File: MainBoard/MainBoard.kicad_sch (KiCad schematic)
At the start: 30 parts, among them U1 V3S, U5 10104110-0001LF, X1 FC-12M32.768KHZ7PF20PPM, X2 X322524MOB4SI

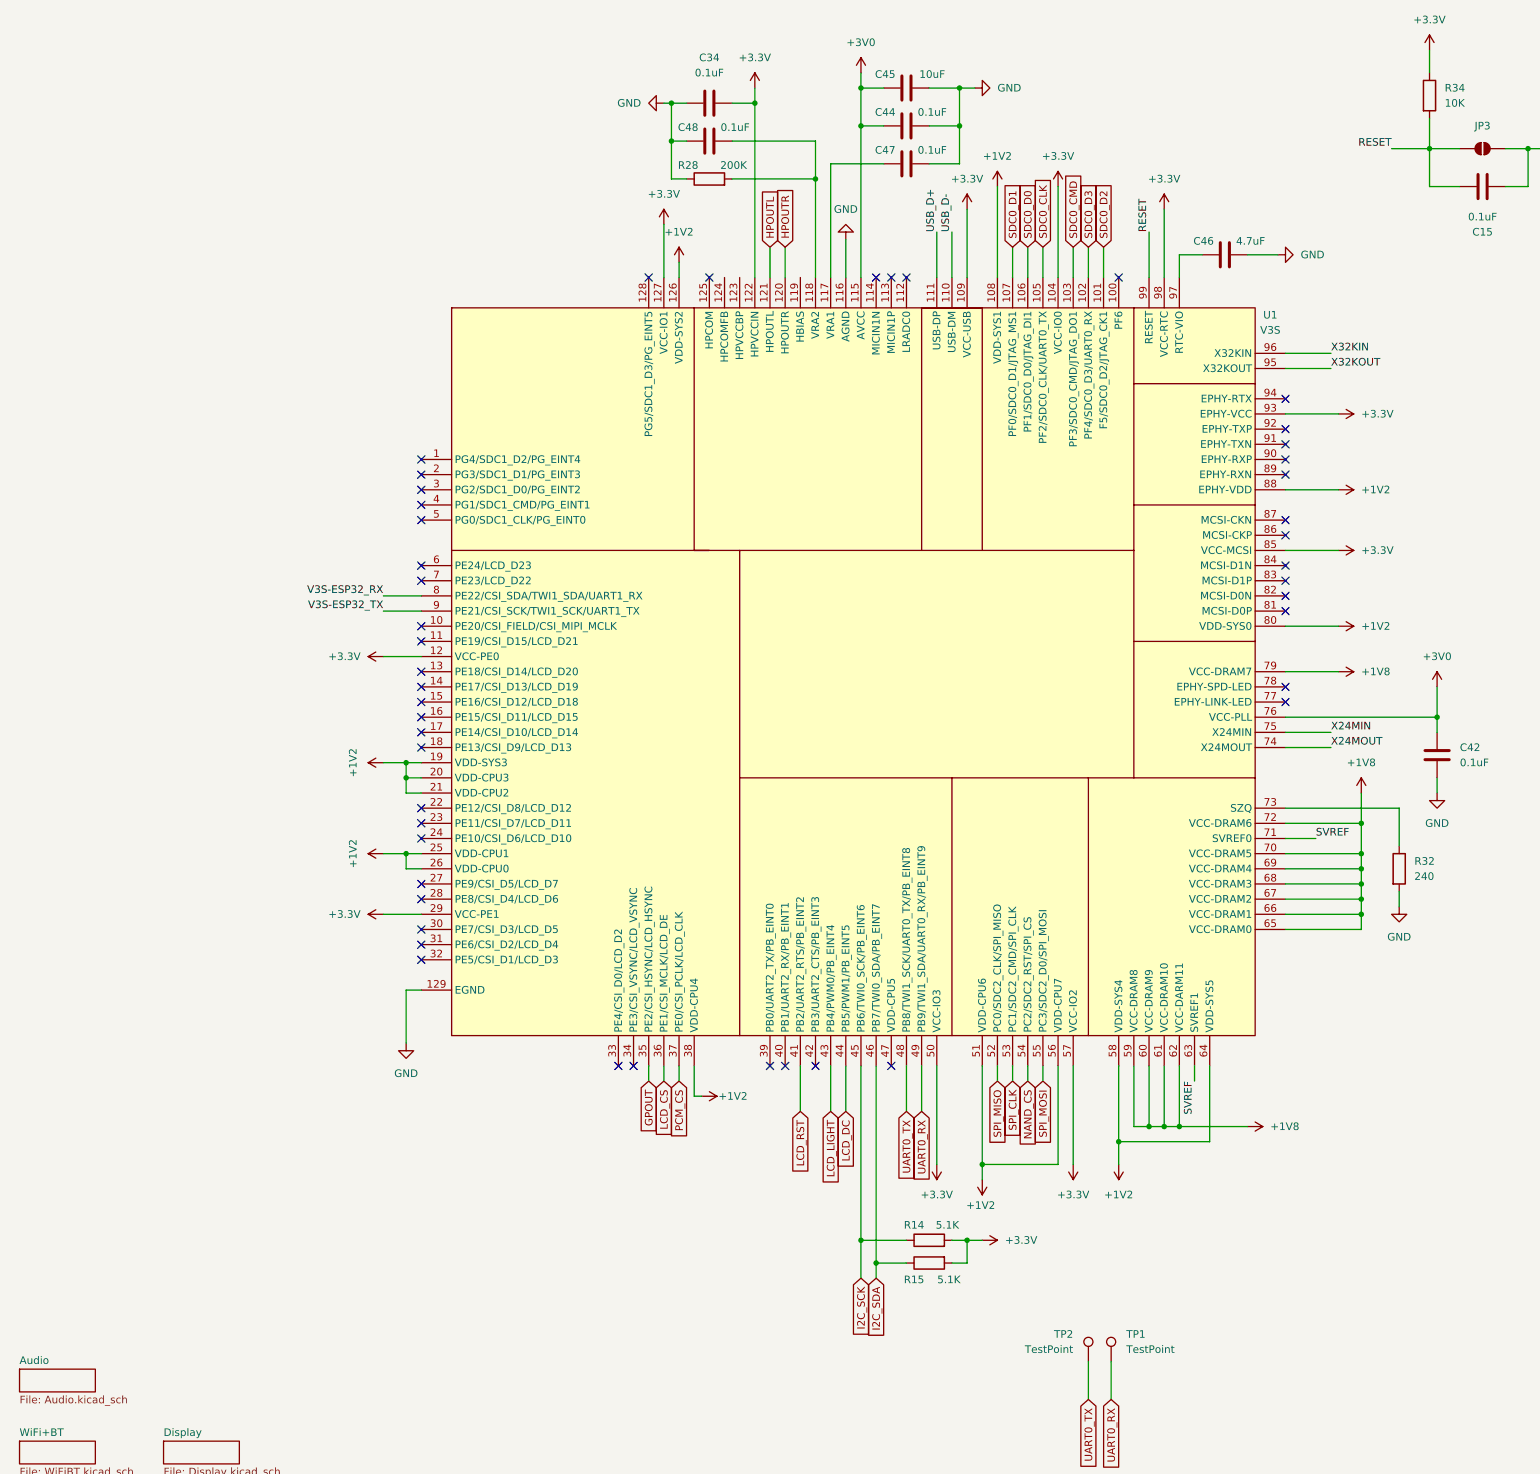
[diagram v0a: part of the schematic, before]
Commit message: footprints for wheel + power changes for v3s
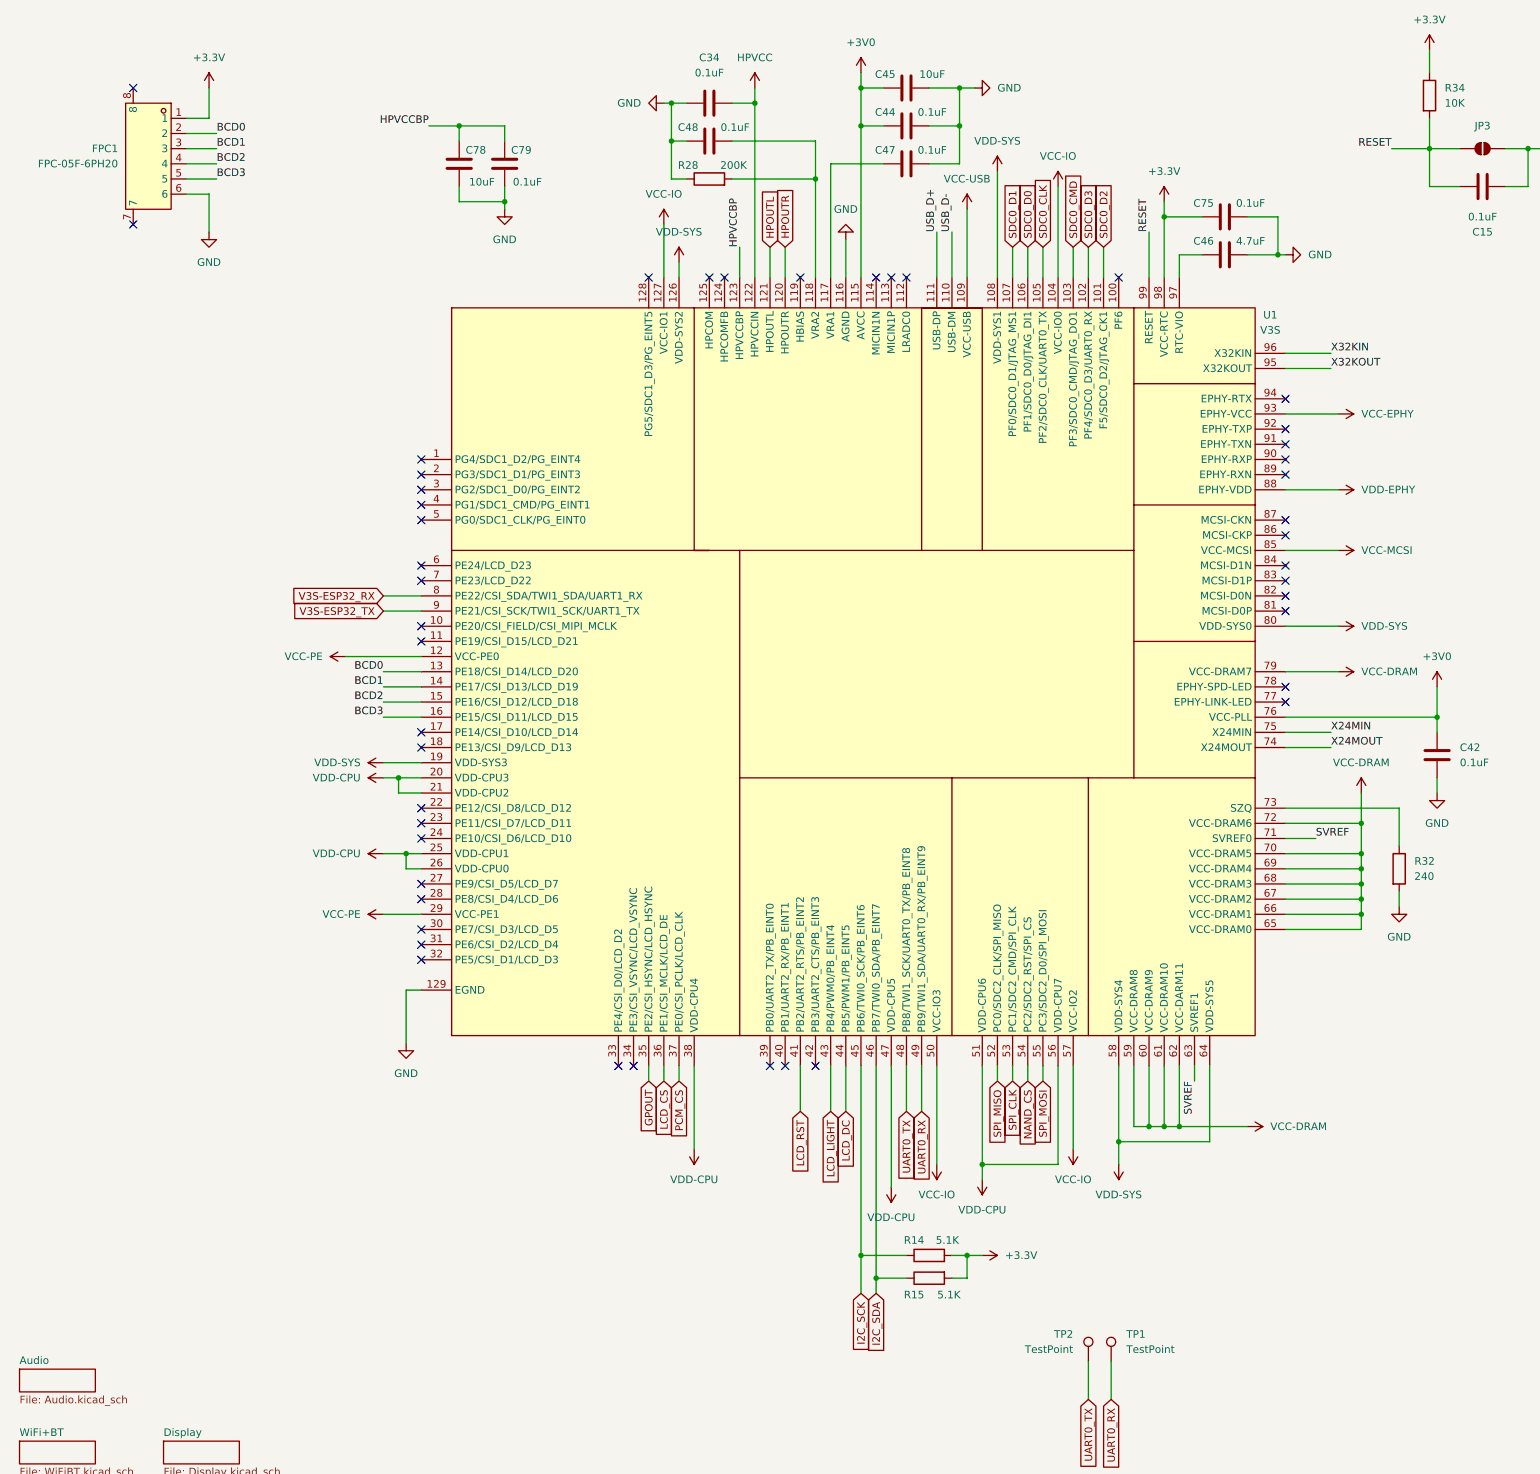
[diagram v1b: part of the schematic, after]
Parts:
- added C75, C79: 0.1uF, symbol Device:C
- added C78: 10uF, symbol Device:C
- added FPC1: FPC-05F-6PH20, easyeda2kicad:FPC-SMD_6P-P0.50_XUNPU_FPC-05F-6PH20, symbol easyeda2kicad:FPC-05F-6PH20
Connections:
- net +1V8: no longer U1.59 (VCC-DRAM8), U1.60 (VCC-DRAM9), U1.61 (VCC-DRAM10), U1.62 (VCC-DARM11), U1.65 (VCC-DRAM0), U1.66 (VCC-DRAM1), U1.67 (VCC-DRAM2), U1.68 (VCC-DRAM3), U1.69 (VCC-DRAM4), U1.70 (VCC-DRAM5), U1.72 (VCC-DRAM6), U1.79 (VCC-DRAM7)
- net +3.3V: now also C75.2, FPC1.1; no longer C34.1, U1.104 (VCC-IO0), U1.109 (VCC-USB), U1.12 (VCC-PE0), U1.122 (HPVCCIN), U1.127 (VCC-IO1), U1.29 (VCC-PE1), U1.50 (VCC-IO3), U1.57 (VCC-IO2), U1.85 (VCC-MCSI), U1.93 (EPHY-VCC)
- net GND: now also C75.1, C78.1, C79.1, FPC1.6
- net HPVCCBP: now reaches U1.123 (HPVCCBP)
- net HPVCCBP: now also C78.2, C79.2
- net BCD0: now reaches U1.13 (PE18/CSI_D14/LCD_D20)
- net BCD0: now also FPC1.2
- net BCD1: now reaches U1.14 (PE17/CSI_D13/LCD_D19)
- net BCD1: now also FPC1.3
- net BCD2: now reaches U1.15 (PE16/CSI_D12/LCD_D18)
- net BCD2: now also FPC1.4
- net BCD3: now reaches U1.16 (PE15/CSI_D11/LCD_D15)
- net BCD3: now also FPC1.5
- net VDD-CPU: now reaches U1.47 (VDD-CPU5)
- net VDD-CPU: now also U1.20 (VDD-CPU3), U1.21 (VDD-CPU2), U1.25 (VDD-CPU1), U1.26 (VDD-CPU0), U1.38 (VDD-CPU4), U1.51 (VDD-CPU6), U1.56 (VDD-CPU7)
- removed net +1V2: U1.108 (VDD-SYS1), U1.126 (VDD-SYS2), U1.19 (VDD-SYS3), U1.20 (VDD-CPU3), U1.21 (VDD-CPU2), U1.25 (VDD-CPU1), U1.26 (VDD-CPU0), U1.38 (VDD-CPU4), U1.51 (VDD-CPU6), U1.56 (VDD-CPU7), U1.58 (VDD-SYS4), U1.64 (VDD-SYS5), U1.80 (VDD-SYS0), U1.88 (EPHY-VDD)
- new net HPVCC: C34.1, U1.122 (HPVCCIN)
- new net VCC-DRAM: U1.59 (VCC-DRAM8), U1.60 (VCC-DRAM9), U1.61 (VCC-DRAM10), U1.62 (VCC-DARM11), U1.65 (VCC-DRAM0), U1.66 (VCC-DRAM1), U1.67 (VCC-DRAM2), U1.68 (VCC-DRAM3), U1.69 (VCC-DRAM4), U1.70 (VCC-DRAM5), U1.72 (VCC-DRAM6), U1.79 (VCC-DRAM7)
- new net VCC-EPHY: U1.93 (EPHY-VCC)
- new net VCC-IO: U1.104 (VCC-IO0), U1.127 (VCC-IO1), U1.50 (VCC-IO3), U1.57 (VCC-IO2)
- new net VCC-MCSI: U1.85 (VCC-MCSI)
- new net VCC-PE: U1.12 (VCC-PE0), U1.29 (VCC-PE1)
- new net VCC-USB: U1.109 (VCC-USB)
- new net VDD-EPHY: U1.88 (EPHY-VDD)
- new net VDD-SYS: U1.108 (VDD-SYS1), U1.126 (VDD-SYS2), U1.19 (VDD-SYS3), U1.58 (VDD-SYS4), U1.64 (VDD-SYS5), U1.80 (VDD-SYS0)
- no-connect marks 48 -> 47
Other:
- moved on the sheet: R14, R15

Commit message: minor power changes
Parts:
- added H1, H2, H3, H4: MountingHole, MountingHole:MountingHole_2.2mm_M2, symbol Mechanical:MountingHole
- C15, C34, C36, C37, C38, C39, C42, C43, C44, C46, C47, C48, C49, C75, C79: footprint (none) -> Capacitor_SMD:C_0402_1005Metric
- C45, C78: footprint (none) -> Capacitor_SMD:C_0603_1608Metric
- JP3: footprint (none) -> Jumper:SolderJumper-2_P1.3mm_Open_Pad1.0x1.5mm
- R14, R15, R21, R26, R27, R28, R29, R32, R34: footprint (none) -> Resistor_SMD:R_0402_1005Metric
- TP1, TP2: footprint (none) -> TestPoint:TestPoint_Pad_1.5x1.5mm

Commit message: layout and starting routing
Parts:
- removed U5: 10104110-0001LF, easyeda2kicad:MICRO-USB-SMD_AMPHENOL_10104110-0001LF, symbol easyeda2kicad:10104110-0001LF
- added USB2: 105164-0001, easyeda2kicad:MICRO-USB-SMD_5P-P0.65-H-F_105164-0001, symbol easyeda2kicad:105164-0001
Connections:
- net BCD0: now also U1.1 (PG4/SDC1_D2/PG_EINT4); no longer U1.13 (PE18/CSI_D14/LCD_D20)
- net BCD1: now also U1.2 (PG3/SDC1_D1/PG_EINT3); no longer U1.14 (PE17/CSI_D13/LCD_D19)
- net BCD2: now also U1.3 (PG2/SDC1_D0/PG_EINT2); no longer U1.15 (PE16/CSI_D12/LCD_D18)
- net BCD3: now also U1.4 (PG1/SDC1_CMD/PG_EINT1); no longer U1.16 (PE15/CSI_D11/LCD_D15)
- net GND: now also USB2.5 (GND), USB2.6 (GND)
- net GPOUT: now also U1.39 (PB0/UART2_TX/PB_EINT0); no longer U1.35 (PE2/CSI_HSYNC/LCD_HSYNC)
- net LCD_CS: now also U1.40 (PB1/UART2_RX/PB_EINT1); no longer U1.36 (PE1/CSI_MCLK/LCD_DE)
- net PCM_CS: now also U1.42 (PB3/UART2_CTS/PB_EINT3); no longer U1.37 (PE0/CSI_PCLK/LCD_CLK)
- net USB_D+: now also USB2.3 (D+)
- net USB_D-: now also USB2.2 (D-)
- net VBUS: now also USB2.1 (VCC)
- net LCD_D21: now reaches U1.11 (PE19/CSI_D15/LCD_D21)
- net LCD_D14: now reaches U1.17 (PE14/CSI_D10/LCD_D14)
- net LCD_D13: now reaches U1.18 (PE13/CSI_D9/LCD_D13)
- net LCD_D12: now reaches U1.22 (PE12/CSI_D8/LCD_D12)
- net LCD_D11: now reaches U1.23 (PE11/CSI_D7/LCD_D11)
- net LCD_D10: now reaches U1.24 (PE10/CSI_D6/LCD_D10)
- net LCD_D7: now reaches U1.27 (PE9/CSI_D5/LCD_D7)
- net LCD_D6: now reaches U1.28 (PE8/CSI_D4/LCD_D6)
- net LCD_D5: now reaches U1.30 (PE7/CSI_D3/LCD_D5)
- net LCD_D4: now reaches U1.31 (PE6/CSI_D2/LCD_D4)
- net LCD_D3: now reaches U1.32 (PE5/CSI_D1/LCD_D3)
- net LCD_D2: now reaches U1.33 (PE4/CSI_D0/LCD_D2)
- net LCD_VSYNC: now reaches U1.34 (PE3/CSI_VSYNC/LCD_VSYNC)
- net LCD_D23: now reaches U1.6 (PE24/LCD_D23)
- net LCD_D22: now reaches U1.7 (PE23/LCD_D22)
- net at R21.2: now also USB2.4 (ID)
- new net LCD_CLK: U1.37 (PE0/CSI_PCLK/LCD_CLK)
- new net LCD_D15: U1.16 (PE15/CSI_D11/LCD_D15)
- new net LCD_D18: U1.15 (PE16/CSI_D12/LCD_D18)
- new net LCD_D19: U1.14 (PE17/CSI_D13/LCD_D19)
- new net LCD_D20: U1.13 (PE18/CSI_D14/LCD_D20)
- new net LCD_DE: U1.36 (PE1/CSI_MCLK/LCD_DE)
- new net LCD_HSYNC: U1.35 (PE2/CSI_HSYNC/LCD_HSYNC)
- no-connect marks 47 -> 25

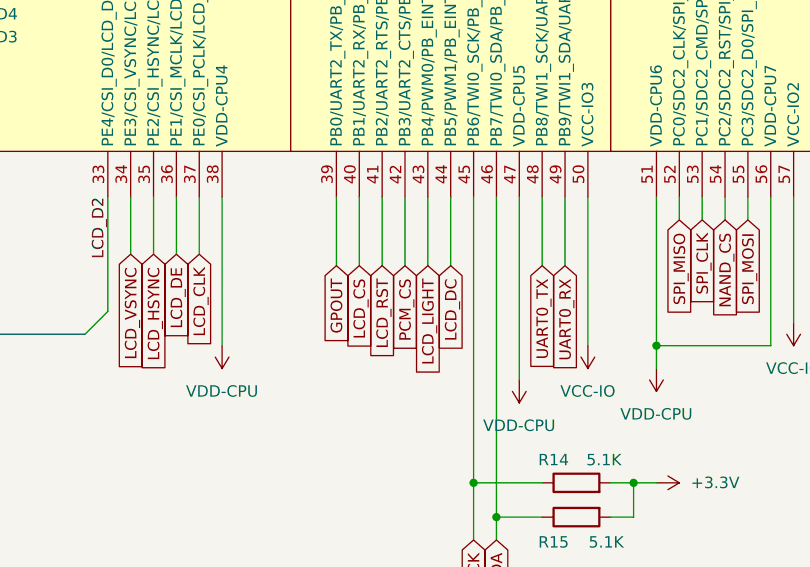
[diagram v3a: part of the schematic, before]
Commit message: routed signals
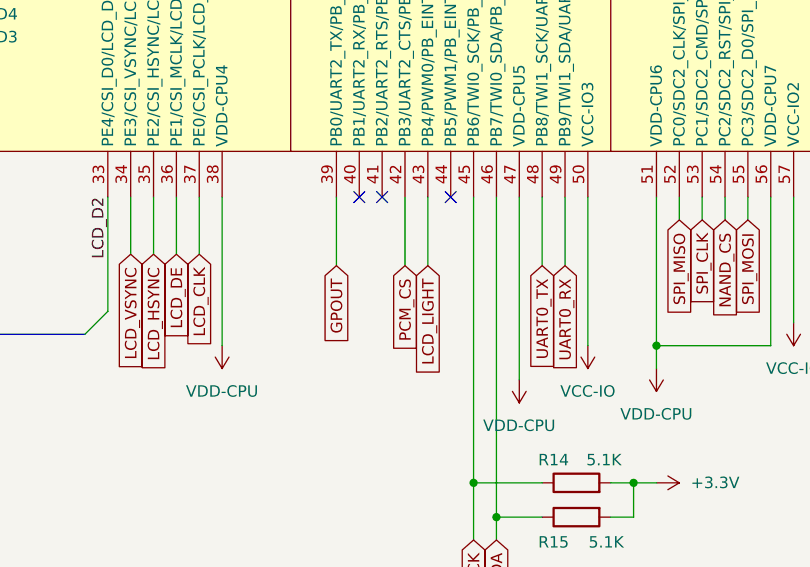
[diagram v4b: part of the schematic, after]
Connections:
- net LCD_CS: no longer names the net of U1.40 (PB1/UART2_RX/PB_EINT1)
- net LCD_DC: no longer names the net of U1.44 (PB5/PWM1/PB_EINT5)
- net LCD_RST: no longer names the net of U1.41 (PB2/UART2_RTS/PB_EINT2)
- no-connect marks 25 -> 28
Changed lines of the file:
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@@
 	)
 	(no_connect
+		(at 146.05 200.66)
+	)
+	(no_connect
 		(at 229.87 109.22)
 	)
@@
 	)
 	(no_connect
+		(at 148.59 200.66)
+	)
+	(no_connect
 		(at 148.59 68.58)
 	)
@@
 	)
 	(no_connect
+		(at 156.21 200.66)
+	)
+	(no_connect
 		(at 229.87 119.38)
 	)
@@
 	(wire
 		(pts
-			(xy 148.59 200.66) (xy 148.59 208.28)
-		)
-		(stroke
-			(width 0)
-			(type default)
-		)
-	)
-	(wire
-		(pts
 			(xy 78.74 124.46) (xy 85.09 124.46)
 		)
@@
 	(wire
 		(pts
-			(xy 156.21 200.66) (xy 156.21 208.28)
-		)
-		(stroke
-			(width 0)
-			(type default)
-		)
-	)
-	(wire
-		(pts
 			(xy 325.12 67.31) (xy 325.12 71.12)
 		)
@@
 	(wire
 		(pts
-			(xy 146.05 200.66) (xy 146.05 208.28)
-		)
-		(stroke
-			(width 0)
-			(type default)
-		)
-	)
-	(wire
-		(pts
 			(xy 189.23 200.66) (xy 189.23 203.2)
 		)
@@
 		)
 	)
-	(global_label "LCD_DC"
-		(shape input)
-		(at 156.21 208.28 270)
-		(fields_autoplaced yes)
-		(effects
-			(font
-				(size 1.27 1.27)
-			)
-			(justify right)
-		)
-		(property "Intersheetrefs" "${INTERSHEET_REFS}"
-			(at 156.21 218.3409 90)
-			(effects
-				(font
-					(size 1.27 1.27)
-				)
-				(justify right)
-				(hide yes)
-			)
-		)
-	)
 	(global_label "GPOUT"
 		(shape input)
@@
 		)
 	)
-	(global_label "LCD_CS"
-		(shape input)
-		(at 146.05 208.28 270)
-		(fields_autoplaced yes)
-		(effects
-			(font
-				(size 1.27 1.27)
-			)
-			(justify right)
-		)
-		(property "Intersheetrefs" "${INTERSHEET_REFS}"
-			(at 146.05 218.2804 90)
-			(effects
-				(font
-					(size 1.27 1.27)
-				)
-				(justify right)
-				(hide yes)
-			)
-		)
-	)
 	(global_label "PCM_CS"
 		(shape input)
@@
 			(effects
 				(font
-					(size 1.27 1.27)
-				)
-				(justify right)
-				(hide yes)
-			)
-		)
-	)
-	(global_label "LCD_RST"
-		(shape input)
-		(at 148.59 208.28 270)
-		(fields_autoplaced yes)
-		(effects
-			(font
-				(size 1.27 1.27)
-			)
-			(justify right)
-		)
-		(property "Intersheetrefs" "${INTERSHEET_REFS}"
-			(at 148.59 219.248 90)
-			(effects
-				(font

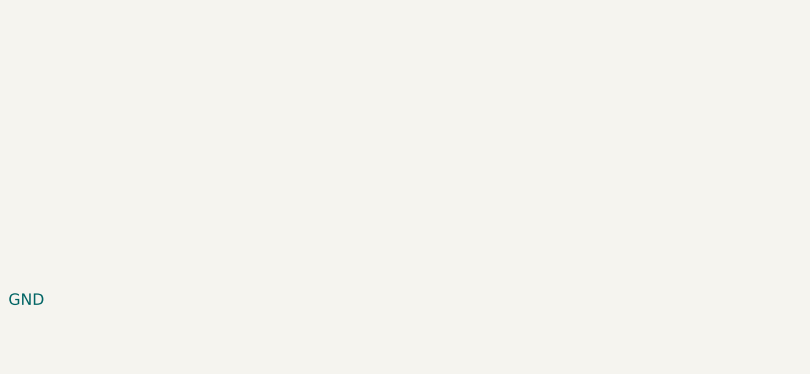
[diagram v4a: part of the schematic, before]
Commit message: added teardrops and voltage probe points
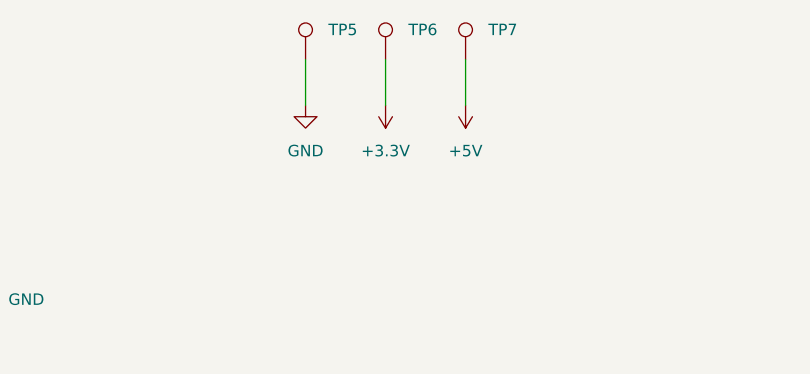
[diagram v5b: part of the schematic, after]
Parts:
- added TP5, TP6, TP7: TestPoint, TestPoint:TestPoint_Pad_1.5x1.5mm, symbol Connector:TestPoint
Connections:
- net +3.3V: now also TP6.1
- net GND: now also TP5.1
- new net +5V: TP7.1
